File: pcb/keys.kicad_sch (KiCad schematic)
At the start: 1 part, among them U7 74HC14

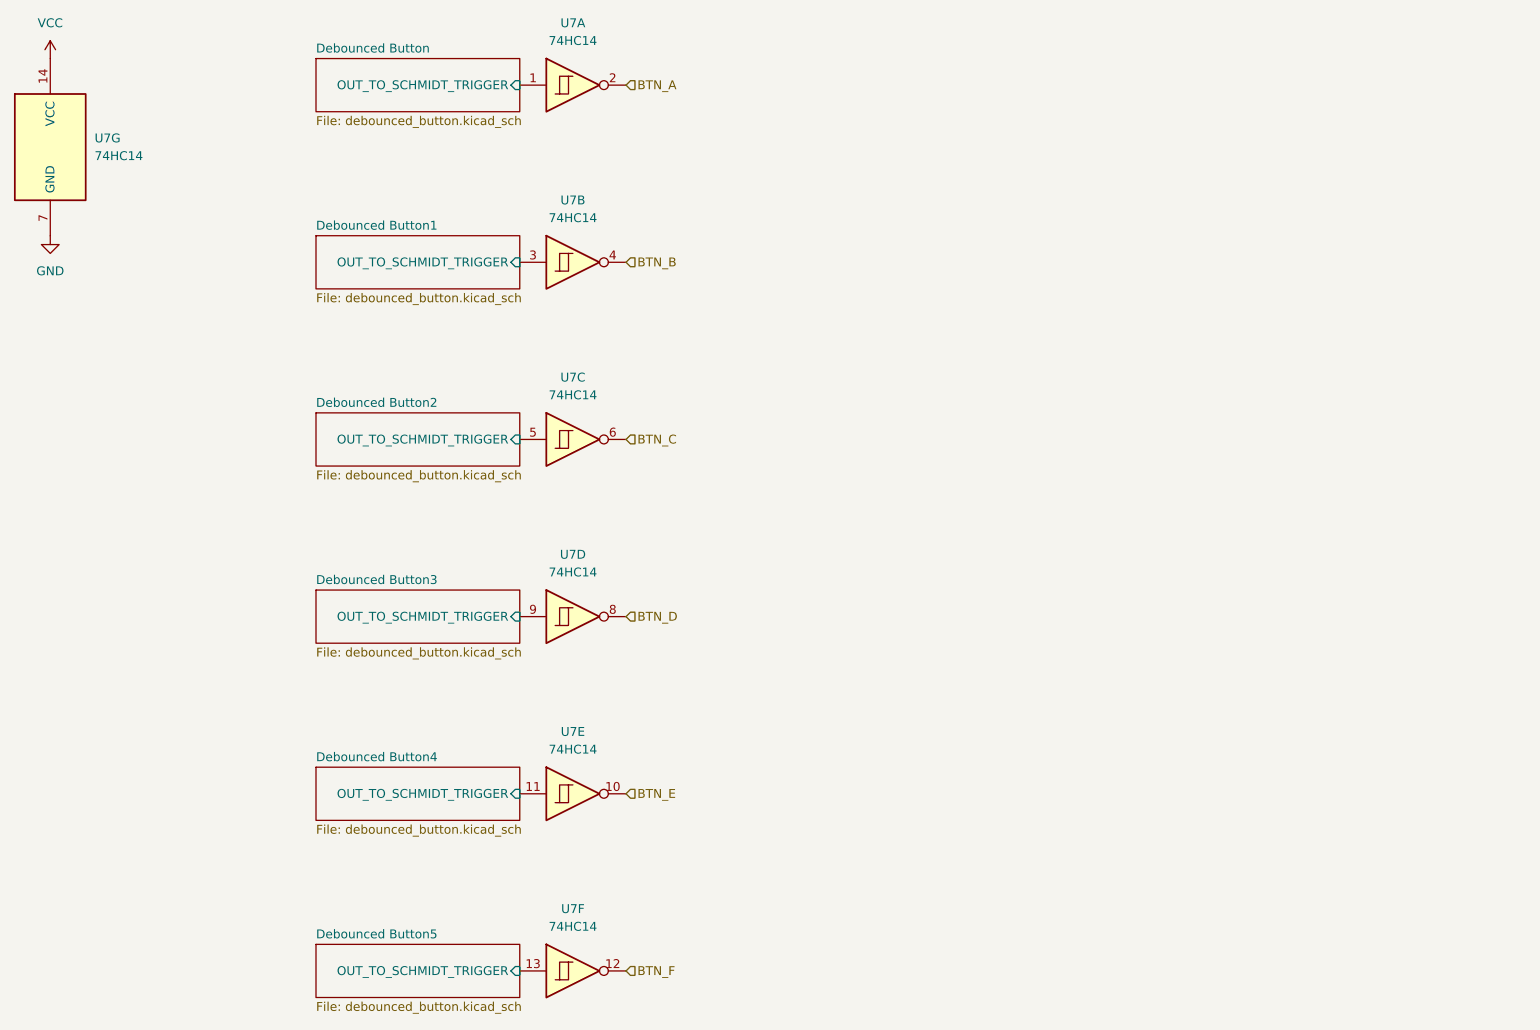
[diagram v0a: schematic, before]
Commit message: expand usb, piano keys, cleanup
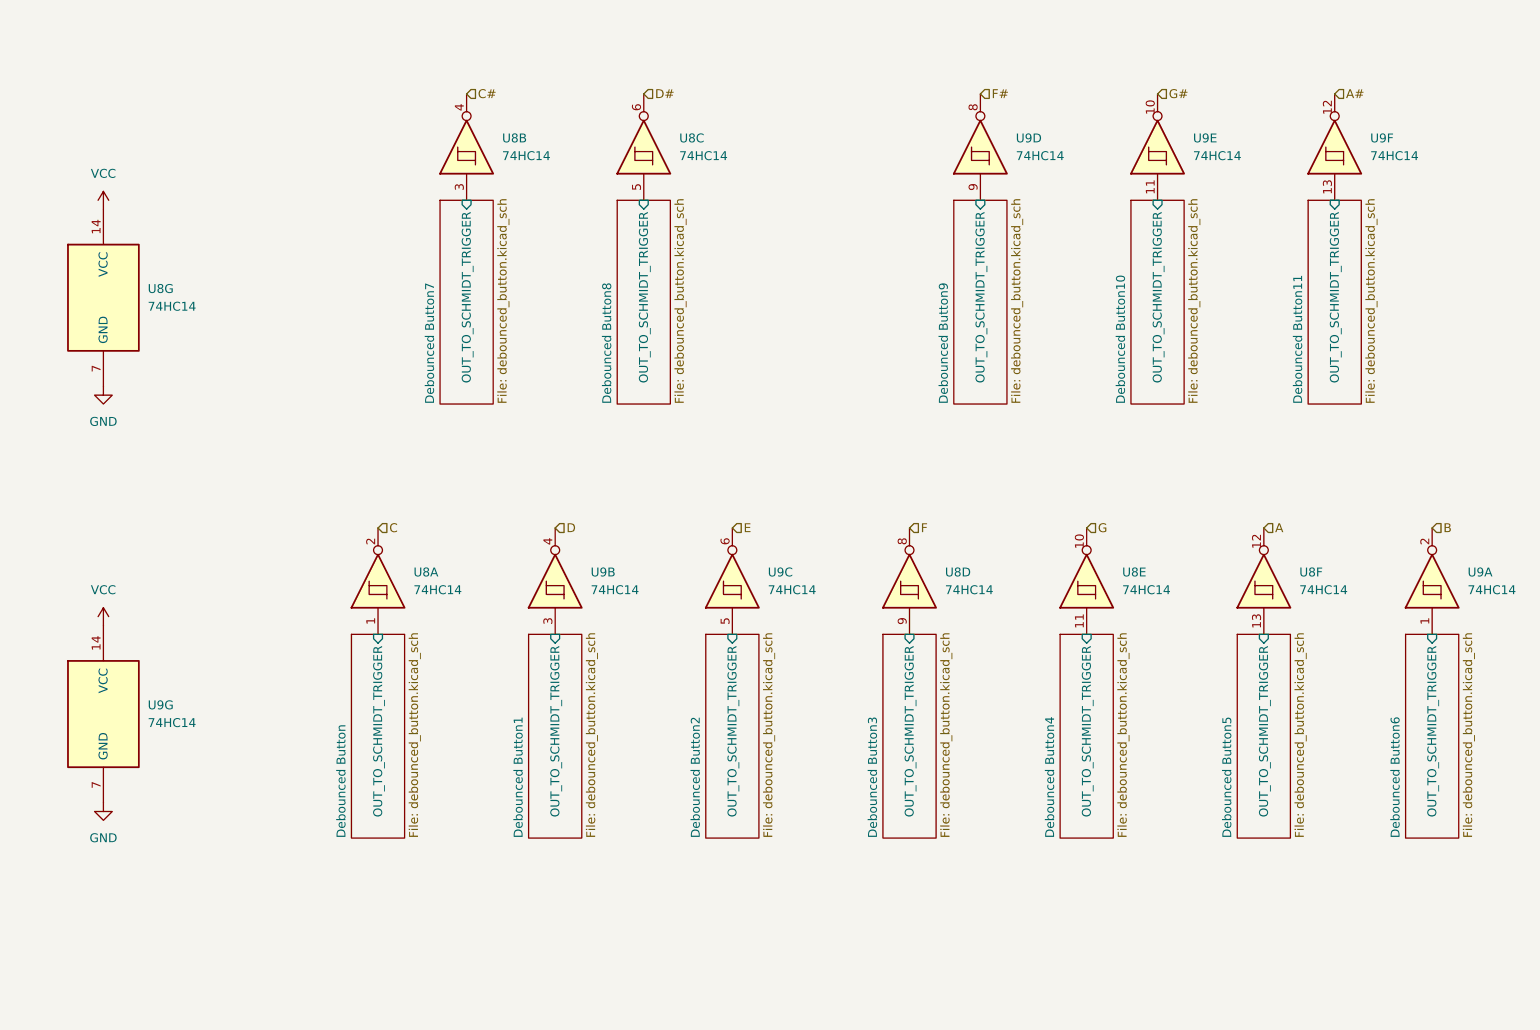
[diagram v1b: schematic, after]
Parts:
- removed U7: 74HC14, Package_SO:SO-14_3.9x8.65mm_P1.27mm, symbol 74xx:74HC14
- added U8, U9: 74HC14, Package_SO:SO-14_3.9x8.65mm_P1.27mm, symbol 74xx:74HC14
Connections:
- net Debounced Button/OUT_TO_SCHMIDT_TRIGGER: now also U8.1
- net Debounced Button1/OUT_TO_SCHMIDT_TRIGGER: now also U9.3
- net Debounced Button2/OUT_TO_SCHMIDT_TRIGGER: now also U9.5
- net Debounced Button3/OUT_TO_SCHMIDT_TRIGGER: now also U8.9
- net Debounced Button4/OUT_TO_SCHMIDT_TRIGGER: now also U8.11
- net Debounced Button5/OUT_TO_SCHMIDT_TRIGGER: now also U8.13
- net GND: now also U8.7 (GND), U9.7 (GND)
- net VCC: now also U8.14 (VCC), U9.14 (VCC)
- new net A: U8.12
- new net A#: U9.12
- new net B: U9.2
- new net C: U8.2
- new net C#: U8.4
- new net D: U9.4
- new net D#: U8.6
- new net Debounced Button10/OUT_TO_SCHMIDT_TRIGGER: U9.11
- new net Debounced Button11/OUT_TO_SCHMIDT_TRIGGER: U9.13
- new net Debounced Button6/OUT_TO_SCHMIDT_TRIGGER: U9.1
- new net Debounced Button7/OUT_TO_SCHMIDT_TRIGGER: U8.3
- new net Debounced Button8/OUT_TO_SCHMIDT_TRIGGER: U8.5
- new net Debounced Button9/OUT_TO_SCHMIDT_TRIGGER: U9.9
- new net E: U9.6
- new net F: U8.8
- new net F#: U9.8
- new net G: U8.10
- new net G#: U9.10
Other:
- added sheet Debounced Button10 (debounced_button.kicad_sch)
- added sheet Debounced Button11 (debounced_button.kicad_sch)
- added sheet Debounced Button6 (debounced_button.kicad_sch)
- added sheet Debounced Button7 (debounced_button.kicad_sch)
- added sheet Debounced Button8 (debounced_button.kicad_sch)
- added sheet Debounced Button9 (debounced_button.kicad_sch)

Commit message: switch back to rp2350, ideal diode OR'ing for power
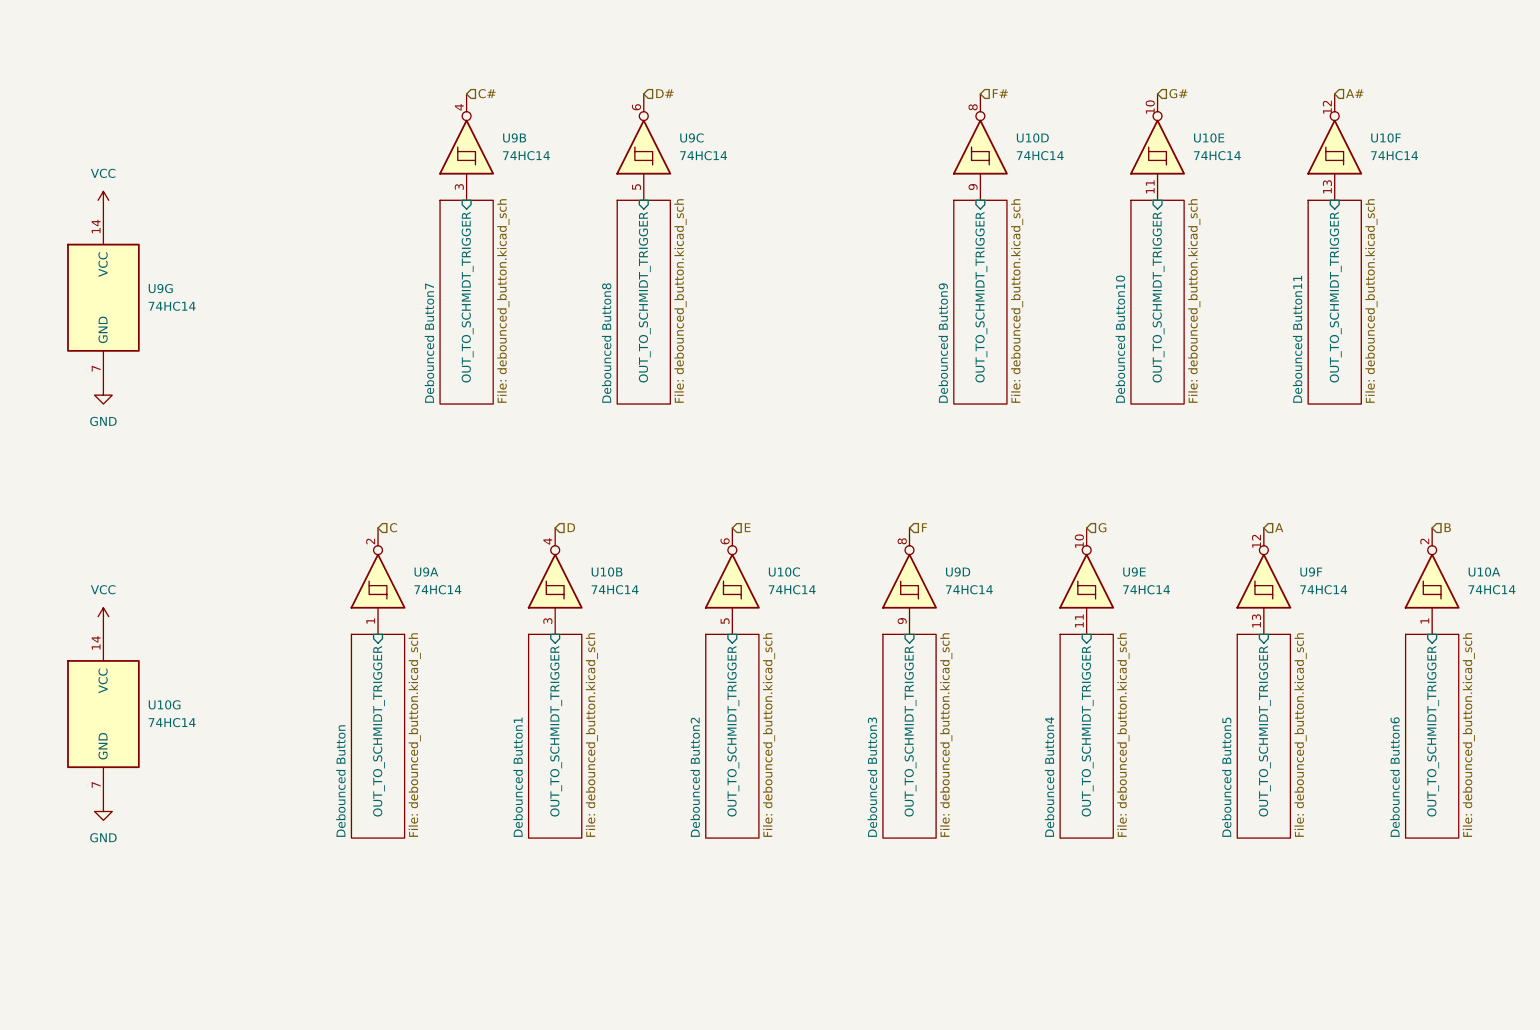
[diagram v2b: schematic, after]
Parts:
- renumbered U9 to U10, U8 to U9
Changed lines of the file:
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@@
 		(dnp no)
 		(fields_autoplaced yes)
-		(property "Reference" "U9"
+		(property "Reference" "U10"
 			(at 113.03 107.9499 90)
 			(effects
@@
 			(project ""
 				(path "/c334e595-b478-4c47-9288-968ac2c472fc/3946e482-0b45-422f-8df8-a9f9b66d3e73"
-					(reference "U9")
+					(reference "U10")
 					(unit 2)
 				)
@@
 		(dnp no)
 		(fields_autoplaced yes)
-		(property "Reference" "#PWR094"
+		(property "Reference" "#PWR0102"
 			(at 43.18 59.69 0)
 			(effects
@@
 			(project ""
 				(path "/c334e595-b478-4c47-9288-968ac2c472fc/3946e482-0b45-422f-8df8-a9f9b66d3e73"
-					(reference "#PWR094")
+					(reference "#PWR0102")
 					(unit 1)
 				)
@@
 		(dnp no)
 		(fields_autoplaced yes)
-		(property "Reference" "#PWR096"
+		(property "Reference" "#PWR0104"
 			(at 43.18 119.38 0)
 			(effects
@@
 			(project ""
 				(path "/c334e595-b478-4c47-9288-968ac2c472fc/3946e482-0b45-422f-8df8-a9f9b66d3e73"
-					(reference "#PWR096")
+					(reference "#PWR0104")
 					(unit 1)
 				)
@@
 		(dnp no)
 		(fields_autoplaced yes)
-		(property "Reference" "U8"
+		(property "Reference" "U9"
 			(at 100.33 45.7199 90)
 			(effects
@@
 			(project ""
 				(path "/c334e595-b478-4c47-9288-968ac2c472fc/3946e482-0b45-422f-8df8-a9f9b66d3e73"
-					(reference "U8")
+					(reference "U9")
 					(unit 2)
 				)
@@
 		(dnp no)
 		(fields_autoplaced yes)
-		(property "Reference" "U8"
+		(property "Reference" "U9"
 			(at 49.53 67.3099 0)
 			(effects
@@
 			(project ""
 				(path "/c334e595-b478-4c47-9288-968ac2c472fc/3946e482-0b45-422f-8df8-a9f9b66d3e73"
-					(reference "U8")
+					(reference "U9")
 					(unit 7)
 				)
@@
 		(dnp no)
 		(fields_autoplaced yes)
-		(property "Reference" "U9"
+		(property "Reference" "U10"
 			(at 224.79 45.7199 90)
 			(effects
@@
 			(project ""
 				(path "/c334e595-b478-4c47-9288-968ac2c472fc/3946e482-0b45-422f-8df8-a9f9b66d3e73"
-					(reference "U9")
+					(reference "U10")
 					(unit 6)
 				)
@@
 		(dnp no)
 		(fields_autoplaced yes)
-		(property "Reference" "U8"
+		(property "Reference" "U9"
 			(at 125.73 45.7199 90)
 			(effects
@@
 			(project ""
 				(path "/c334e595-b478-4c47-9288-968ac2c472fc/3946e482-0b45-422f-8df8-a9f9b66d3e73"
-					(reference "U8")
+					(reference "U9")
 					(unit 3)
 				)
@@
 		(dnp no)
 		(fields_autoplaced yes)
-		(property "Reference" "U9"
+		(property "Reference" "U10"
 			(at 173.99 45.7199 90)
 			(effects
@@
 			(project ""
 				(path "/c334e595-b478-4c47-9288-968ac2c472fc/3946e482-0b45-422f-8df8-a9f9b66d3e73"
-					(reference "U9")
+					(reference "U10")
 					(unit 4)
 				)
@@
 		(dnp no)
 		(fields_autoplaced yes)
-		(property "Reference" "U8"
+		(property "Reference" "U9"
 			(at 214.63 107.9499 90)
 			(effects
@@
 			(project ""
 				(path "/c334e595-b478-4c47-9288-968ac2c472fc/3946e482-0b45-422f-8df8-a9f9b66d3e73"
-					(reference "U8")
+					(reference "U9")
 					(unit 6)
 				)
@@
 		(dnp no)
 		(fields_autoplaced yes)
-		(property "Reference" "#PWR095"
+		(property "Reference" "#PWR0103"
 			(at 43.18 87.63 0)
 			(effects
@@
 			(project ""
 				(path "/c334e595-b478-4c47-9288-968ac2c472fc/3946e482-0b45-422f-8df8-a9f9b66d3e73"
-					(reference "#PWR095")
+					(reference "#PWR0103")
 					(unit 1)
 				)
@@
 		(dnp no)
 		(fields_autoplaced yes)
-		(property "Reference" "U8"
+		(property "Reference" "U9"
 			(at 87.63 107.9499 90)
 			(effects
@@
 			(project ""
 				(path "/c334e595-b478-4c47-9288-968ac2c472fc/3946e482-0b45-422f-8df8-a9f9b66d3e73"
-					(reference "U8")
+					(reference "U9")
 					(unit 1)
 				)
@@
 		(dnp no)
 		(fields_autoplaced yes)
-		(property "Reference" "#PWR097"
+		(property "Reference" "#PWR0105"
 			(at 43.18 147.32 0)
 			(effects
@@
 			(project ""
 				(path "/c334e595-b478-4c47-9288-968ac2c472fc/3946e482-0b45-422f-8df8-a9f9b66d3e73"
-					(reference "#PWR097")
+					(reference "#PWR0105")
 					(unit 1)
 				)
@@
 		(dnp no)
 		(fields_autoplaced yes)
-		(property "Reference" "U8"
+		(property "Reference" "U9"
 			(at 189.23 107.9499 90)
 			(effects
@@
 			(project ""
 				(path "/c334e595-b478-4c47-9288-968ac2c472fc/3946e482-0b45-422f-8df8-a9f9b66d3e73"
-					(reference "U8")
+					(reference "U9")
 					(unit 5)
 				)
@@
 		(dnp no)
 		(fields_autoplaced yes)
-		(property "Reference" "U8"
+		(property "Reference" "U9"
 			(at 163.83 107.9499 90)
 			(effects
@@
 			(project ""
 				(path "/c334e595-b478-4c47-9288-968ac2c472fc/3946e482-0b45-422f-8df8-a9f9b66d3e73"
-					(reference "U8")
+					(reference "U9")
 					(unit 4)
 				)
@@
 		(dnp no)
 		(fields_autoplaced yes)
-		(property "Reference" "U9"
+		(property "Reference" "U10"
 			(at 49.53 126.9999 0)
 			(effects
@@
 			(project ""
 				(path "/c334e595-b478-4c47-9288-968ac2c472fc/3946e482-0b45-422f-8df8-a9f9b66d3e73"
-					(reference "U9")
+					(reference "U10")
 					(unit 7)
 				)
@@
 		(dnp no)
 		(fields_autoplaced yes)
-		(property "Reference" "U9"
+		(property "Reference" "U10"
 			(at 138.43 107.9499 90)
 			(effects
@@
 			(project ""
 				(path "/c334e595-b478-4c47-9288-968ac2c472fc/3946e482-0b45-422f-8df8-a9f9b66d3e73"
-					(reference "U9")
+					(reference "U10")
 					(unit 3)
 				)
@@
 		(dnp no)
 		(fields_autoplaced yes)
-		(property "Reference" "U9"
+		(property "Reference" "U10"
 			(at 199.39 45.7199 90)
 			(effects
@@
 			(project ""
 				(path "/c334e595-b478-4c47-9288-968ac2c472fc/3946e482-0b45-422f-8df8-a9f9b66d3e73"
-					(reference "U9")
+					(reference "U10")
 					(unit 5)
 				)
@@
 		(dnp no)
 		(fields_autoplaced yes)
-		(property "Reference" "U9"
+		(property "Reference" "U10"
 			(at 238.76 107.9499 90)
 			(effects
@@
 			(project ""
 				(path "/c334e595-b478-4c47-9288-968ac2c472fc/3946e482-0b45-422f-8df8-a9f9b66d3e73"
-					(reference "U9")
+					(reference "U10")
 					(unit 1)
 				)
